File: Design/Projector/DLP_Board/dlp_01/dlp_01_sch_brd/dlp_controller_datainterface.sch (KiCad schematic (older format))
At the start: 6 parts

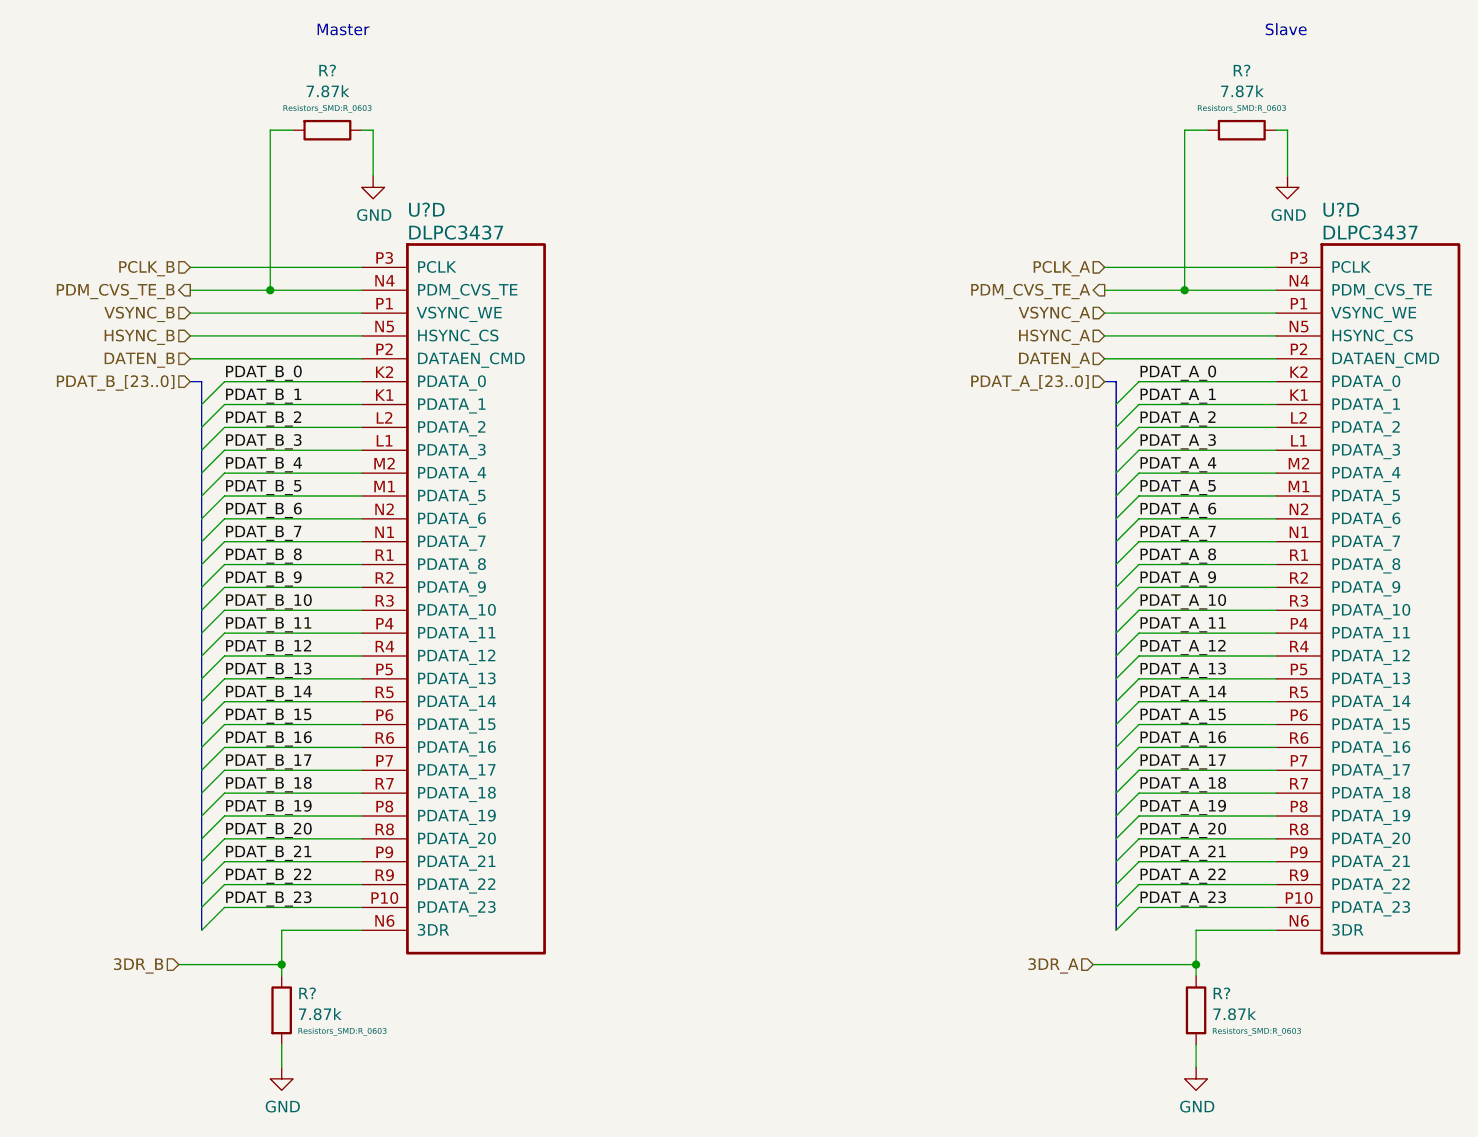
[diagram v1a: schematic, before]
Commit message: Initial placement of power converters, BGA fanout and Z-turn board outline imported
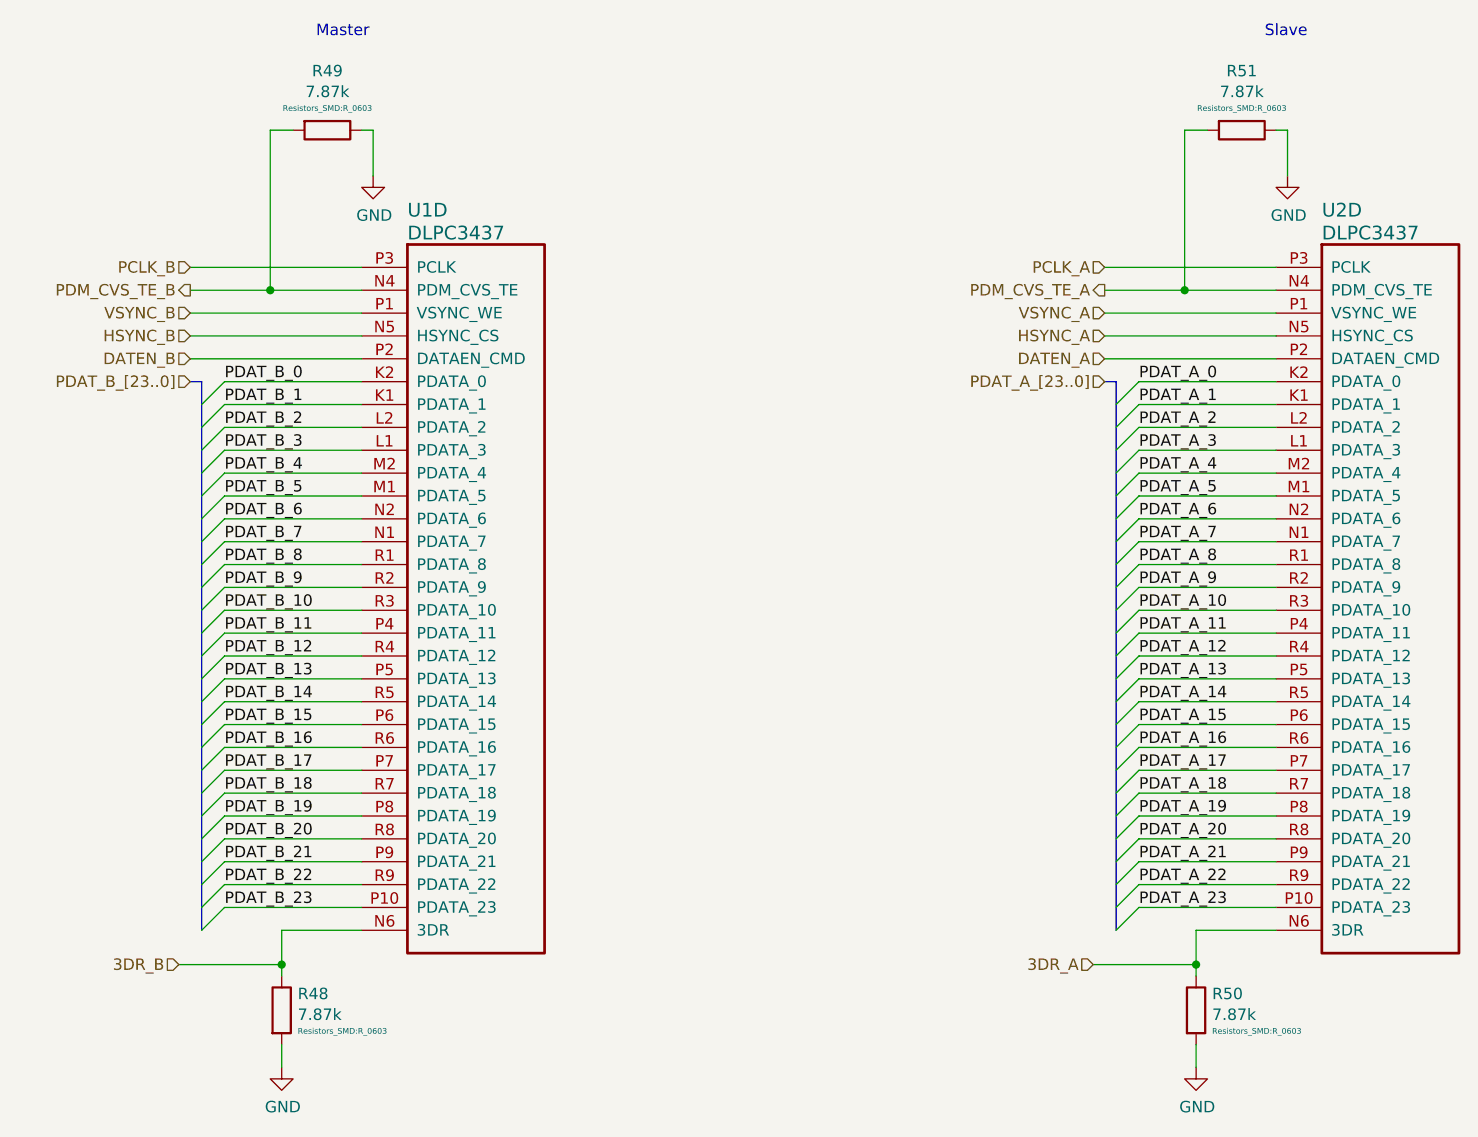
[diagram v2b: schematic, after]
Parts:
- gave numbers to parts that had none: 6
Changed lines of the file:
@@
 $Descr A3 16535 11693
 encoding utf-8
-Sheet 6 10
+Sheet 6 11
 Title "DLP Controller Data Interface"
 Date ""
@@
 $EndDescr
 $Comp
-L Device:R R?
+L Device:R R48
 U 1 1 5E8FA7FC
 P 5900 7350
-F 0 "R?" H 5970 7422 50  0000 L CNN
+F 0 "R48" H 5970 7422 50  0000 L CNN
 F 1 "7.87k" H 5970 7331 50  0000 L CNN
 F 2 "Resistors_SMD:R_0603" H 5970 7259 25  0000 L CNN
@@
 $EndComp
 $Comp
-L power:GND #PWR?
+L power:GND #PWR046
 U 1 1 5E8FBDE2
 P 5900 7600
-F 0 "#PWR?" H 5900 7350 50  0001 C CNN
+F 0 "#PWR046" H 5900 7350 50  0001 C CNN
 F 1 "GND" H 5905 7427 50  0000 C CNN
 F 2 "" H 5900 7600 50  0001 C CNN
@@
 	5900 7200 5900 7150
 $Comp
-L Device:R R?
+L Device:R R49
 U 1 1 5E8FC7AE
 P 6100 3500
-F 0 "R?" V 5841 3500 50  0000 C CNN
+F 0 "R49" V 5841 3500 50  0000 C CNN
 F 1 "7.87k" V 5932 3500 50  0000 C CNN
 F 2 "Resistors_SMD:R_0603" V 6004 3500 25  0000 C CNN
@@
 $EndComp
 $Comp
-L power:GND #PWR?
+L power:GND #PWR047
 U 1 1 5E8FE7BE
 P 6300 3700
-F 0 "#PWR?" H 6300 3450 50  0001 C CNN
+F 0 "#PWR047" H 6300 3450 50  0001 C CNN
 F 1 "GND" H 6305 3527 50  0000 C CNN
 F 2 "" H 6300 3700 50  0001 C CNN
@@
 	5650 4600 6250 4600
 $Comp
-L TexasInstruments_DLP:DLPC3437 U?
+L TexasInstruments_DLP:DLPC3437 U1
 U 4 1 5E8F23F1
 P 6250 4100
-F 0 "U?" H 6450 4350 60  0000 L CNN
+F 0 "U1" H 6450 4350 60  0000 L CNN
 F 1 "DLPC3437" H 6450 4250 60  0000 L CNN
 F 2 "ZEZ0201A:BGA-225_15x15_13.1x13.1mm" H 7250 4450 50  0001 C CNN
@@
 PDAT_B_23
 $Comp
-L Device:R R?
+L Device:R R50
 U 1 1 5E95C735
 P 9900 7350
-F 0 "R?" H 9970 7422 50  0000 L CNN
+F 0 "R50" H 9970 7422 50  0000 L CNN
 F 1 "7.87k" H 9970 7331 50  0000 L CNN
 F 2 "Resistors_SMD:R_0603" H 9970 7259 25  0000 L CNN
@@
 $EndComp
 $Comp
-L power:GND #PWR?
+L power:GND #PWR048
 U 1 1 5E95C73F
 P 9900 7600
-F 0 "#PWR?" H 9900 7350 50  0001 C CNN
+F 0 "#PWR048" H 9900 7350 50  0001 C CNN
 F 1 "GND" H 9905 7427 50  0000 C CNN
 F 2 "" H 9900 7600 50  0001 C CNN
@@
 	9900 7200 9900 7150
 $Comp
-L Device:R R?
+L Device:R R51
 U 1 1 5E95C74B
 P 10100 3500
-F 0 "R?" V 9841 3500 50  0000 C CNN
+F 0 "R51" V 9841 3500 50  0000 C CNN
 F 1 "7.87k" V 9932 3500 50  0000 C CNN
 F 2 "Resistors_SMD:R_0603" V 10004 3500 25  0000 C CNN
@@
 $EndComp
 $Comp
-L power:GND #PWR?
+L power:GND #PWR049
 U 1 1 5E95C755
 P 10300 3700
-F 0 "#PWR?" H 10300 3450 50  0001 C CNN
+F 0 "#PWR049" H 10300 3450 50  0001 C CNN
 F 1 "GND" H 10305 3527 50  0000 C CNN
 F 2 "" H 10300 3700 50  0001 C CNN
@@
 	9650 4600 10250 4600
 $Comp
-L TexasInstruments_DLP:DLPC3437 U?
+L TexasInstruments_DLP:DLPC3437 U2
 U 4 1 5E95C774
 P 10250 4100
-F 0 "U?" H 10450 4350 60  0000 L CNN
+F 0 "U2" H 10450 4350 60  0000 L CNN
 F 1 "DLPC3437" H 10450 4250 60  0000 L CNN
 F 2 "ZEZ0201A:BGA-225_15x15_13.1x13.1mm" H 11250 4450 50  0001 C CNN

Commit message: Schematic and PCB complete ready for review
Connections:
- net 3DR_A: no longer names the net of R50.1, U2.N6 (3DR)
- net 3DR_B: no longer names the net of R48.1, U1.N6 (3DR)
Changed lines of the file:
@@
 Wire Wire Line
 	5900 7600 5900 7500
-Wire Wire Line
-	5900 7200 5900 7150
 $Comp
 L Device:R R49
@@
 Wire Wire Line
 	9900 7600 9900 7500
-Wire Wire Line
-	9900 7200 9900 7150
 $Comp
 L Device:R R51
@@
 Text Notes 6050 3100 0    50   ~ 0
 Master
-Text HLabel 9450 7150 0    50   Input ~ 0
-3DR_A
-Wire Wire Line
-	9450 7150 9900 7150
-Connection ~ 9900 7150
-Wire Wire Line
-	9900 7150 9900 7000
-Text HLabel 5450 7150 0    50   Input ~ 0
-3DR_B
-Wire Wire Line
-	5450 7150 5900 7150
-Connection ~ 5900 7150
-Wire Wire Line
-	5900 7150 5900 7000
+Wire Wire Line
+	9900 7000 9900 7200
+Wire Wire Line
+	5900 7000 5900 7200
 Wire Bus Line
 	5550 4600 5550 7000
